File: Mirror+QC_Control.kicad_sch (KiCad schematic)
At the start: 71 parts, among them J2 Screw_Terminal_01x04, J3 Screw_Terminal_01x06, J4 FSM DRIVER, U1 LT1012, U10 LT1012, U11 LT1012, U2 LM4040DBZ-2.0, U3 LT1012, U5 LT1012, U6 LT1012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

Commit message: removing fake FSM connector, must solder digikey components
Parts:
- J4: LCSC C7501289 -> (none)
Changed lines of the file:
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@@
-			)
-		)
-		(property "LCSC" "C7501289 "
-			(at 234.95 139.7 0)
-			(effects
-				(font
-					(size 1.27 1.27)
-				)
-				(hide yes)
 			)
 		)

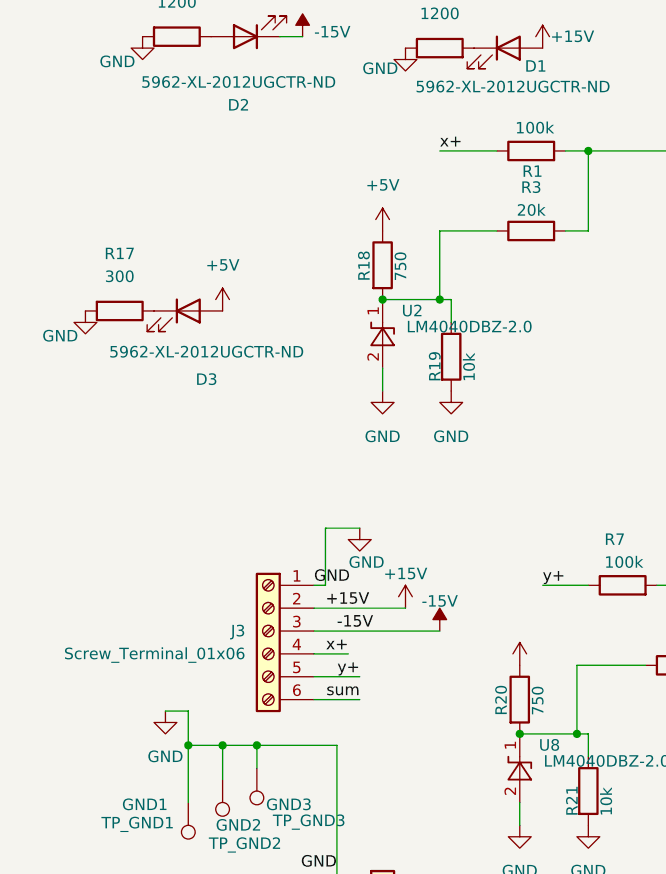
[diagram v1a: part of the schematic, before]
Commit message: rearranged board for enclosure compatability
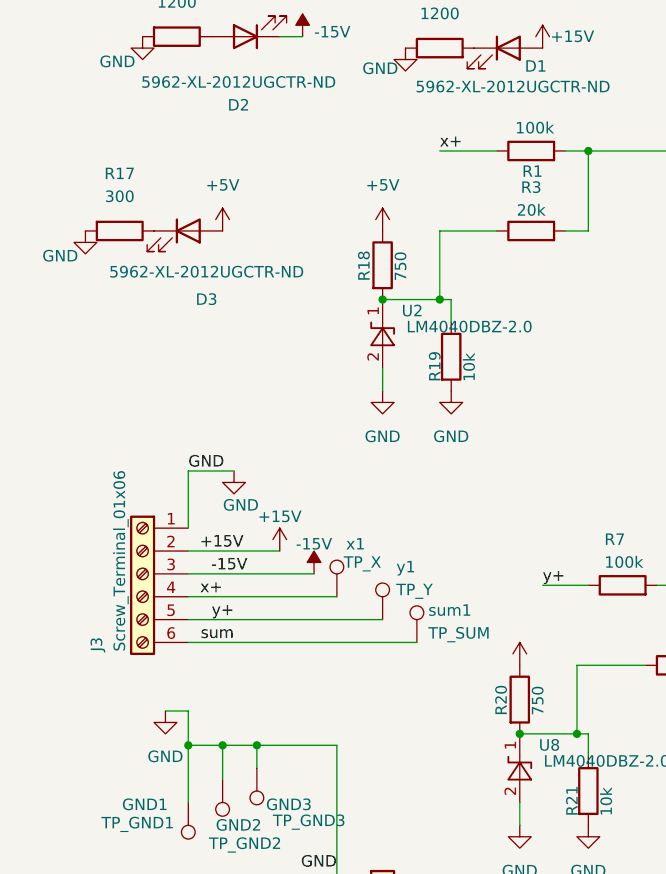
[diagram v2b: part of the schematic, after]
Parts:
- added sum1: TP_SUM, TestPoint:TestPoint_Loop_D2.60mm_Drill1.6mm_Beaded, symbol Connector:TestPoint
- added x1: TP_X, TestPoint:TestPoint_Loop_D2.60mm_Drill1.6mm_Beaded, symbol Connector:TestPoint
- added y1: TP_Y, TestPoint:TestPoint_Loop_D2.60mm_Drill1.6mm_Beaded, symbol Connector:TestPoint
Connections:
- net sum: now also sum1.1
- net x+: now also x1.1
- net y+: now also y1.1
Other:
- moved on the sheet: D3, J3, R17

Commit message: second file for 2QC and 2FSM
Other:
- added sheet Opamps (opamps.kicad_sch)
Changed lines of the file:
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@@
+		)
+	)
+	(sheet
+		(at 33.02 160.02)
+		(size 21.59 13.97)
+		(exclude_from_sim no)
+		(in_bom yes)
+		(on_board yes)
+		(dnp no)
+		(fields_autoplaced yes)
+		(stroke
+			(width 0.1524)
+			(type solid)
+		)
+		(fill
+			(color 0 0 0 0.0000)
+		)
+		(property "Sheetname" "Opamps"
+			(at 33.02 159.3084 0)
+			(effects
+				(font
+					(size 1.27 1.27)
+				)
+				(justify left bottom)
+			)
+		)
+		(property "Sheetfile" "opamps.kicad_sch"
+			(at 33.02 174.5746 0)
+			(effects
+				(font
+					(size 1.27 1.27)
+				)
+				(justify left top)
+			)
+		)
+		(pin "Ystage_2" input
+			(at 33.02 165.1 180)
+			(effects
+				(font
+					(size 1.27 1.27)
+				)
+				(justify left)
+			)
+		)
+		(instances
+			(project "Mirror+QC_Control"
+				(path "/55210a8f-c262-436d-8f74-777787918746"
+					(page "2")
+				)
+			)
 		)
 	)
